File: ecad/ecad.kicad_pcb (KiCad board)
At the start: 4 copper layers, 130.5 x 112.7 mm, 120 parts, among them J1 JTAG, J2 USB_C, J3 Display, Q2 SS8050, SW1 Kailh choc v2, SW10 RotaryEncoder_Switch, SW11 RotaryEncoder_Switch, SW12 Kailh choc v2, SW13 Kailh choc v2, SW14 Kailh choc v2, SW15 RESET, SW16 Kailh choc v2, SW17 Kailh choc v2, SW18 Kailh choc v2, SW19 Kailh choc v2, SW2 Kailh choc v2, SW20 Kailh choc v2, SW21 Kailh choc v2, SW22 Kailh choc v2, SW23 Kailh choc v2, SW24 Kailh choc v2, SW25 Kailh choc v2, SW3 Kailh choc v2, SW4 Kailh choc v2, SW5 Kailh choc v2, SW6 Kailh choc v2, SW7 Kailh choc v2, SW8 Kailh choc v2, SW9 Kailh choc v2, U1 AP2112K-3.3, U2 RP2040, U4 SN74LV1T34DBV, U5 W25Q128JVP, Y1 12MHz

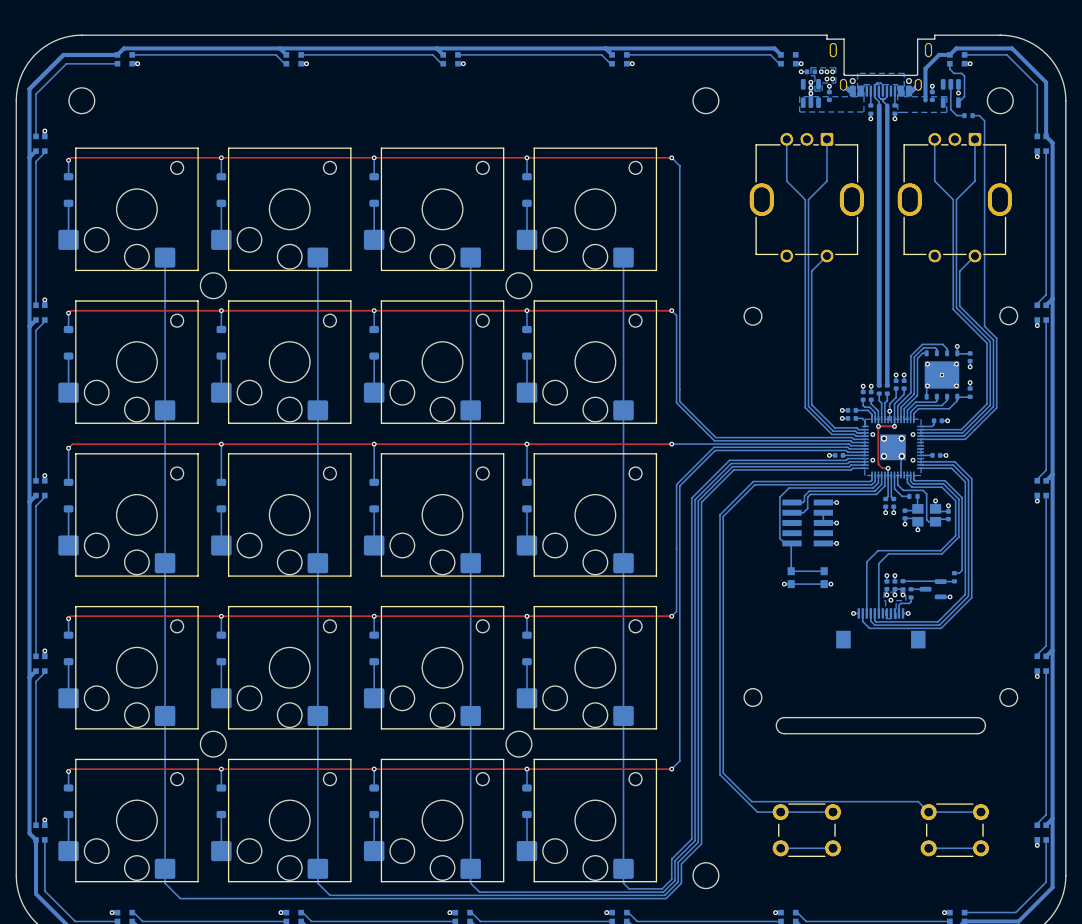
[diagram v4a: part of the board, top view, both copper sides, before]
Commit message: fix(ecad): change pcb dimensions
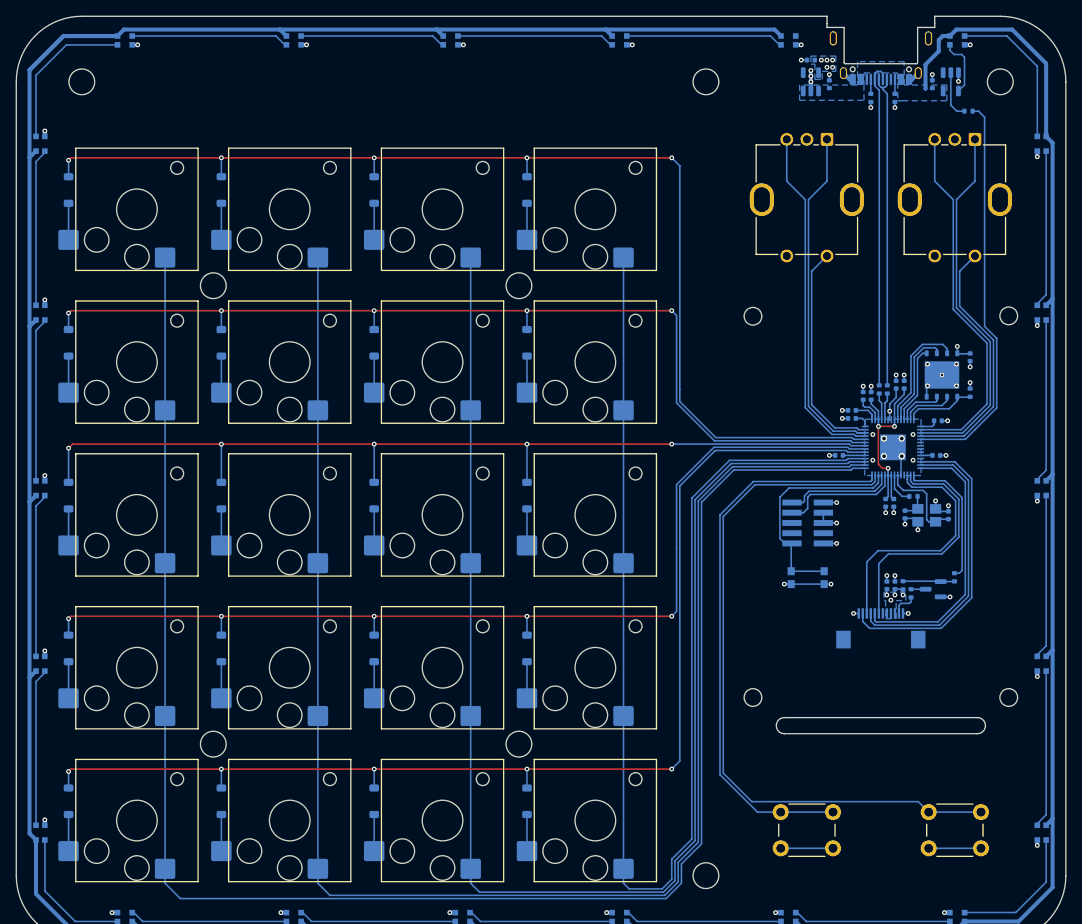
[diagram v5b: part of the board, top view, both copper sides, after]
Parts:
- moved H11 2.35 mm to (71.3, 71.0)
- moved H12 2.35 mm to (148.9, 71.0)
- moved H5 2.35 mm to (185.6, 71.0)
- moved D32 2.35 mm to (180.2, 65.9)
- moved D41 2.35 mm to (117.2, 65.9)
- moved D42 2.35 mm to (76.7, 65.9)
- moved D45 2.35 mm to (138.2, 65.9)
- moved D46 2.35 mm to (159.2, 65.9)
- moved D48 2.35 mm to (97.7, 65.9)
- moved C1 1.45 mm to (164.3, 71.3)
- moved C18 1.45 mm to (177.1, 71.3)
- moved C2 1.45 mm to (162.0, 68.3)
- moved J2 1.45 mm to (170.7, 65.6)
- moved R5 1.45 mm to (169.4, 73.0)
- moved R6 1.45 mm to (172.4, 73.0)
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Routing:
- net +5V: track 479.5 -> 484.8 mm
- net Net-(D29-DIN): track 17.0 -> 19.3 mm
- net Net-(D27-DOUT): track 17.0 -> 19.3 mm
- net Net-(J2-D+-PadA6): track 38.5 -> 40.0 mm
- net Net-(J2-D--PadA7): track 39.5 -> 41.0 mm
- net Net-(D32-DIN): track 6.46 -> 7.35 mm
- net Net-(U4-A): track 5.15 -> 6.04 mm
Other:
- board size 130.5 x 112.7 mm -> 130.5 x 115 mm

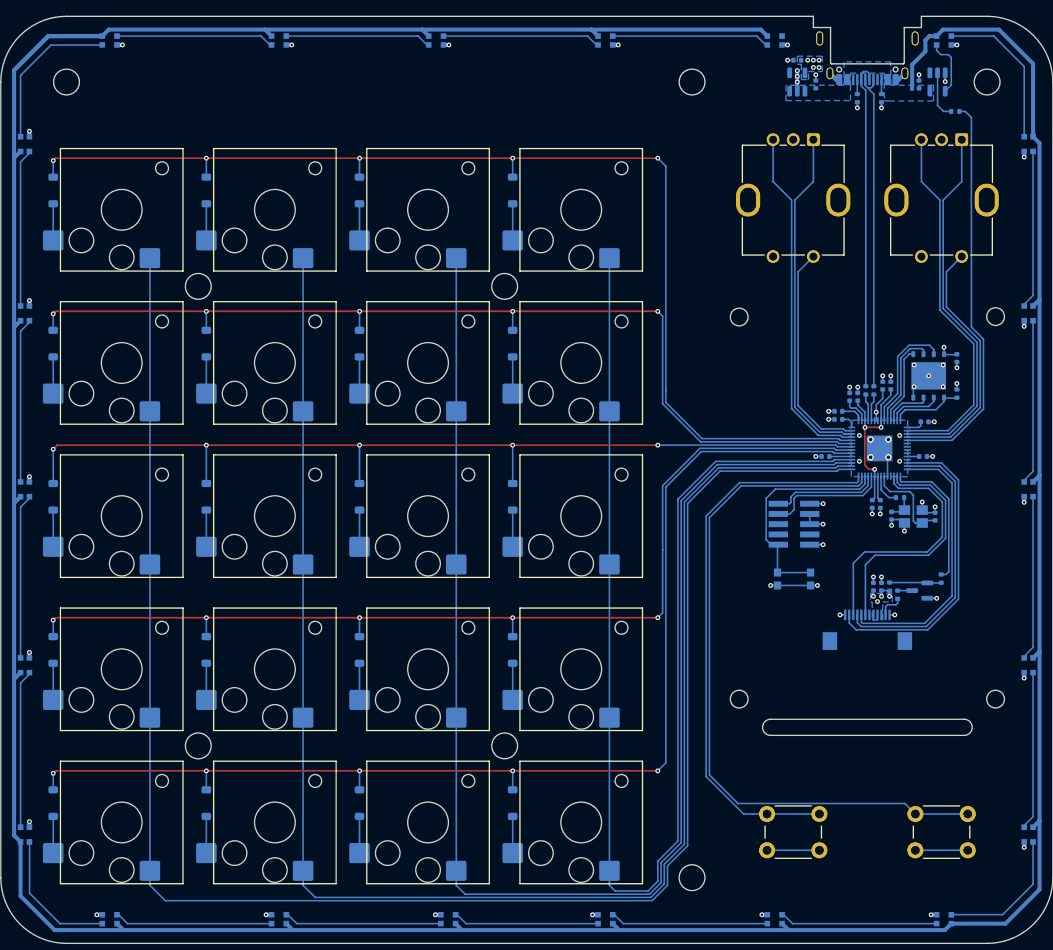
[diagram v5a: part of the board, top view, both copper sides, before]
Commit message: fix(ecad): change board dimensions
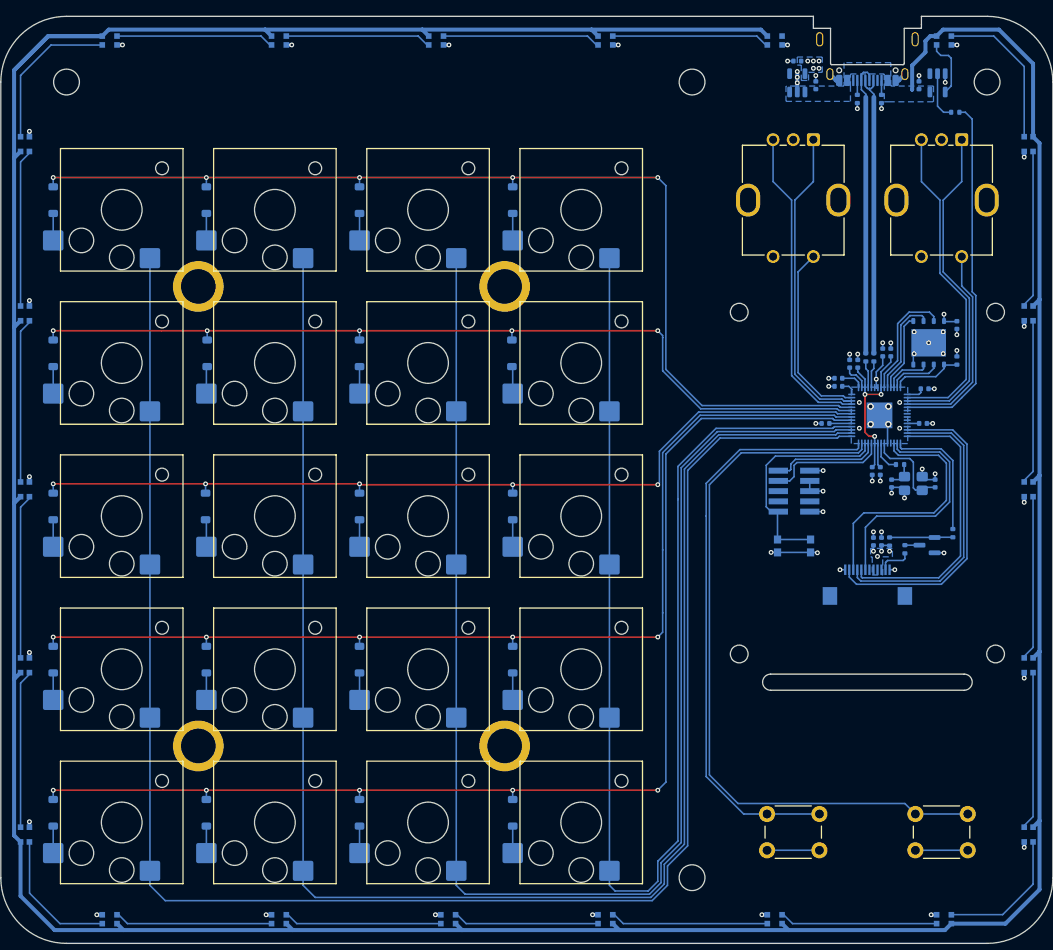
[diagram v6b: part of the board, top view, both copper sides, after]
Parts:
- H1, H2, H3, H4: footprint MountingHole:MountingHole_3.2mm_M3_DIN965 -> sinhoo-smtso3030ctj:smtso3030ctj
- Y1: footprint Crystal:Crystal_SMD_Abracon_ABM8AIG-4Pin_3.2x2.5mm -> Crystal:Crystal_SMD_Abracon_ABM8G-4Pin_3.2x2.5mm
- moved R12 5.82 mm to (181.3, 127.0)
- moved R11 5.71 mm to (175.3, 129.0)
- moved Q2 5.71 mm to (178.1, 128.5)
- moved C19 5.60 mm to (171.4, 128.1)
- moved C9 5.60 mm to (172.4, 128.1)
- moved H7 5.60 mm to (154.8, 142.0)
- moved H8 5.60 mm to (186.6, 142.0)
- moved J3 5.60 mm to (170.7, 133.4)
- moved R13 5.60 mm to (173.4, 128.1)
- moved kibuzzard-68D9895D 5.60 mm to (161.2, 134.3)
- moved C10 4.10 mm to (177.8, 109.1)
- moved C11 4.10 mm to (167.1, 107.8)
- moved C13 4.10 mm to (173.6, 104.6)
- moved C14 4.10 mm to (171.3, 119.3)
- moved C15 4.10 mm to (179.1, 120.8)
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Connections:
- net Net-(J2-D+-PadA6) renamed D+
- net Net-(J2-D--PadA7) renamed D-
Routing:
- net /Switches/R1: track 139.9 -> 128.8 mm
- net /Switches/R2: track 121.4 -> 110.3 mm
- net /Switches/R3: track 117.9 -> 109.7 mm
- net Net-(U2-GPIO2): track 31.8 -> 25.4 mm
- net /Leds/DIN: track 49.7 -> 44.7 mm
- net Net-(U2-GPIO1): track 45.8 -> 41.0 mm
- net Net-(U2-GPIO0): track 45.2 -> 40.3 mm
- net D-: track 41.0 -> 36.8 mm
- net D+: track 40.0 -> 35.8 mm
- net /Switches/C4: track 214.1 -> 218.2 mm
- net /Switches/C3: track 194.9 -> 199.0 mm
- net Net-(U2-GPIO28): track 43.5 -> 39.4 mm
- net Net-(U2-GPIO27): track 43.2 -> 39.1 mm
- net Net-(U2-GPIO29): track 27.2 -> 23.1 mm
- net Net-(U2-GPIO16): track 87.5 -> 91.6 mm
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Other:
- outline, holes or cut-outs redrawn
